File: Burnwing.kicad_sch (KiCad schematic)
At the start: 41 parts, among them J1 USB Type C, J2 Conn_01x06_MountingPin, J3 Conn_01x02_Pin, Q1 NCV8402ADDR2G, Q2 AONR21307, U1 HUSB238

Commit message: Cleaned schematic a bit
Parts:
- removed R15, R16: 750, Resistor_SMD:R_0603_1608Metric_Pad0.98x0.95mm_HandSolder, symbol Library:R
- renumbered D2 to D1, D1 to D2
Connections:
- net GND: now also D1.1 (K), D2.1 (K)
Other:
- moved on the sheet: 12V1, 1A1, 2A1, 5V1, 9V1, Burn1, Burn2, C1, C2, C3, C4, D1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

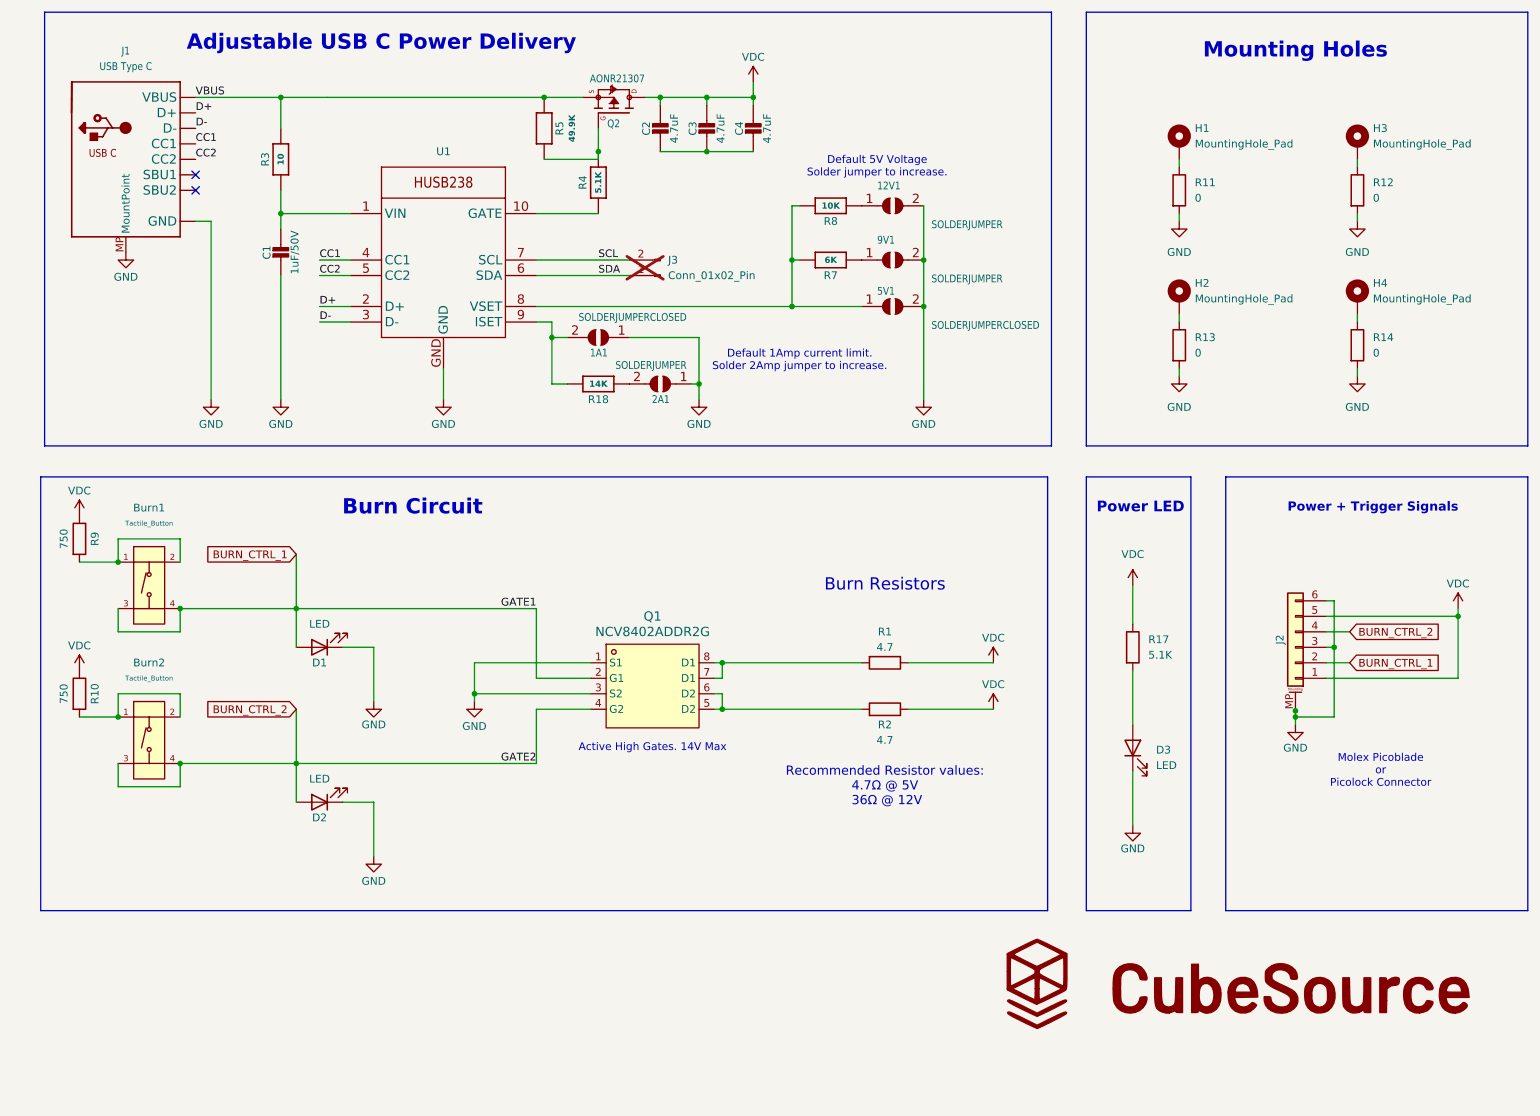
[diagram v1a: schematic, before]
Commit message: Reworked usb power and cleaned up layout
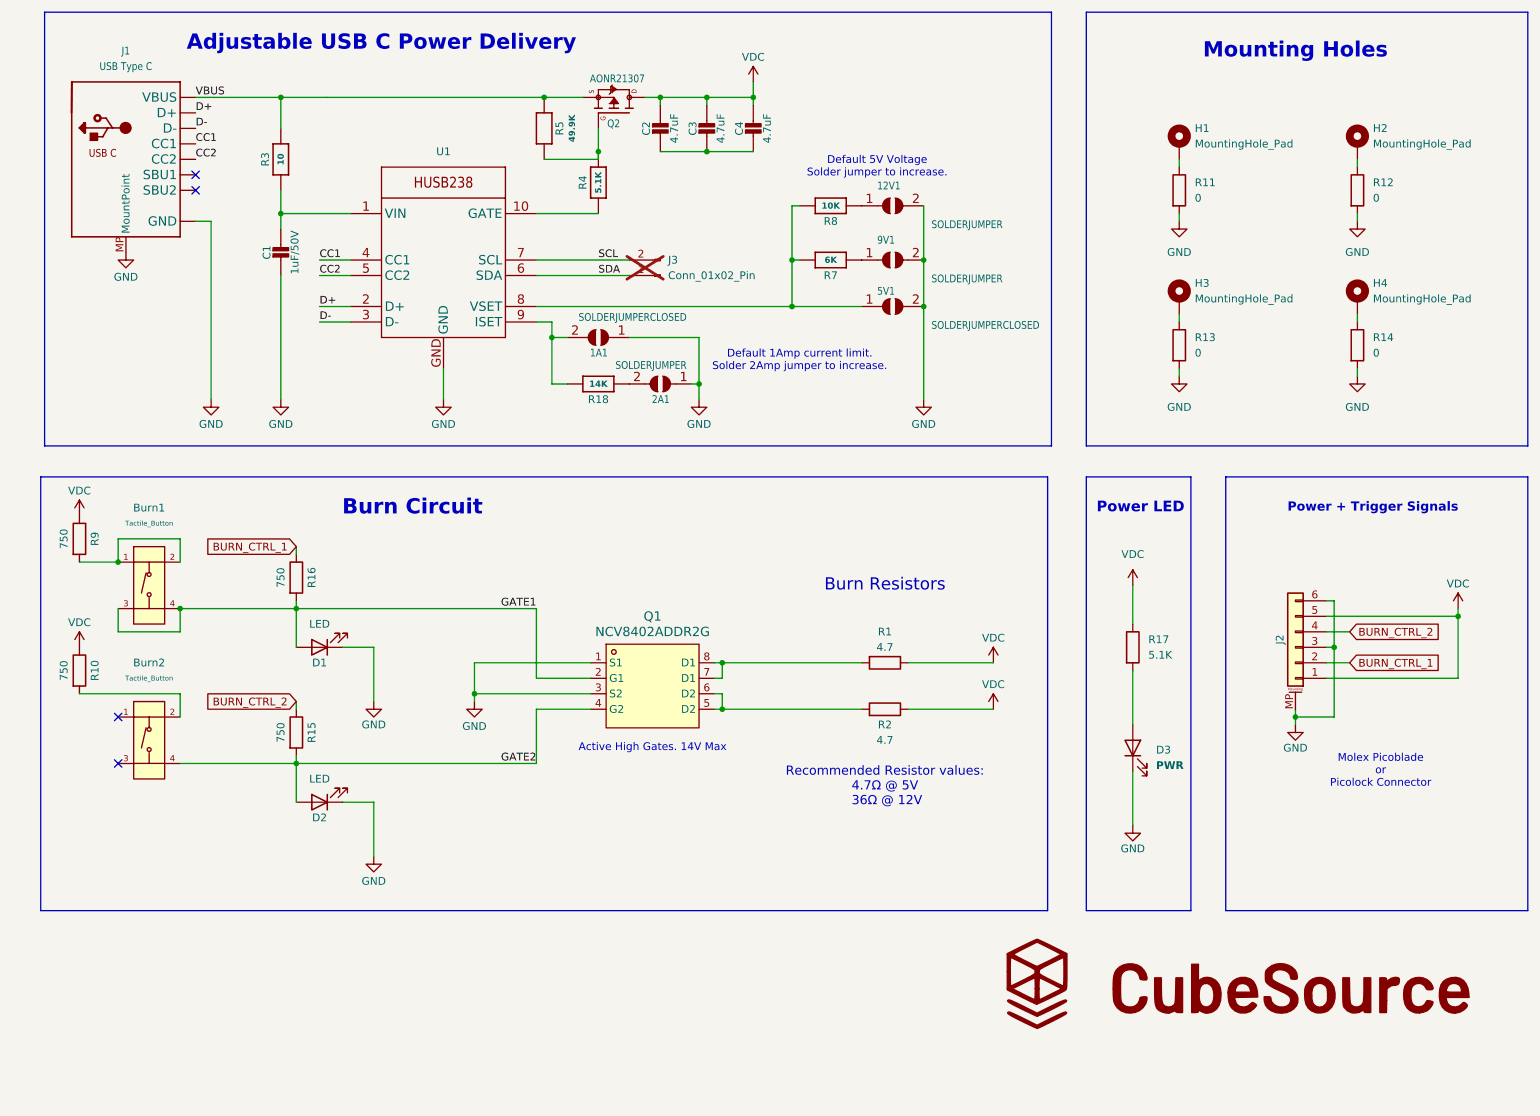
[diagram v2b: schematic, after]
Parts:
- added R15, R16: 750, Resistor_SMD:R_0603_1608Metric_Pad0.98x0.95mm_HandSolder, symbol Library:R
- D3: value LED -> PWR
- renumbered H3 to H2, H2 to H3
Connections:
- net BURN_CTRL_1: now also R16.1; no longer Burn1.3 (C), Burn1.4 (D), D1.2 (A), Q1.2 (G1)
- net BURN_CTRL_2: now also R15.1; no longer Burn2.3 (C), Burn2.4 (D), D2.2 (A), Q1.4 (G2)
- net at Burn2.2 (B), R10.2: no longer Burn2.1 (A)
- new net GATE1: Burn1.3 (C), Burn1.4 (D), D1.2 (A), Q1.2 (G1), R16.2
- new net GATE2: Burn2.4 (D), D2.2 (A), Q1.4 (G2), R15.2
- no-connect marks 2 -> 4
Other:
- moved on the sheet: R10

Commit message: Make some traces widers and added decals
Increased Trace width near R1 and R2 thru holes.

Also added decals
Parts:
- 12V1, 2A1, 9V1: footprint Adafruit HUSB238 USB-C PD Breakout:SOLDERJUMPER_ARROW_NOPASTE -> Library:SOLDERJUMPER_ARROW_NOPASTE
- 1A1, 5V1: footprint Adafruit HUSB238 USB-C PD Breakout:SOLDERJUMPER_CLOSEDWIRE -> Library:SOLDERJUMPER_CLOSEDWIRE
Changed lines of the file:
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@@
 			)
 		)
-		(property "Footprint" "Adafruit HUSB238 USB-C PD Breakout:SOLDERJUMPER_ARROW_NOPASTE"
+		(property "Footprint" "Library:SOLDERJUMPER_ARROW_NOPASTE"
 			(at 157.48 60.96 0)
 			(effects
@@
 			)
 		)
-		(property "Footprint" "Adafruit HUSB238 USB-C PD Breakout:SOLDERJUMPER_CLOSEDWIRE"
+		(property "Footprint" "Library:SOLDERJUMPER_CLOSEDWIRE"
 			(at 109.22 73.66 0)
 			(effects
@@
 			)
 		)
-		(property "Footprint" "Adafruit HUSB238 USB-C PD Breakout:SOLDERJUMPER_ARROW_NOPASTE"
+		(property "Footprint" "Library:SOLDERJUMPER_ARROW_NOPASTE"
 			(at 119.38 81.28 0)
 			(effects
@@
 			)
 		)
-		(property "Footprint" "Adafruit HUSB238 USB-C PD Breakout:SOLDERJUMPER_ARROW_NOPASTE"
+		(property "Footprint" "Library:SOLDERJUMPER_ARROW_NOPASTE"
 			(at 157.48 52.07 0)
 			(effects
@@
 			)
 		)
-		(property "Footprint" "Adafruit HUSB238 USB-C PD Breakout:SOLDERJUMPER_CLOSEDWIRE"
+		(property "Footprint" "Library:SOLDERJUMPER_CLOSEDWIRE"
 			(at 157.48 68.58 0)
 			(effects

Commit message: 4 layer v3 template
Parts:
- removed 9V1: SOLDERJUMPER, Library:SOLDERJUMPER_ARROW_NOPASTE, symbol Library:microbuilder_SOLDERJUMPER
- removed Q1: NCV8402ADDR2G, EasyEDA:SOIC-8_L4.9-W3.9-P1.27-LS6.0-BL, symbol EasyEDA:NCV8402ADDR2G
- removed R10, R9: 750, Resistor_SMD:R_0603_1608Metric_Pad0.98x0.95mm_HandSolder, symbol Library:R
- removed R7: 6K, Resistor_SMD:R_0603_1608Metric_Pad0.98x0.95mm_HandSolder, symbol Library:microbuilder_RESISTOR_0603_NOOUT
- added U2: BTS7030-2EPA, EasyEDA:PG-TSDSO-14_L4.9-W3.9-P0.65-LS6.0-BL-EP, symbol EasyEDA:BTS7030-2EPA
- Burn1, Burn2: value Tactile_Button -> KEY-SMD_4P-L6.0-W6.0-P4.50-LS9.5-BR; footprint PCM_JLCPCB:SW-SMD_4P-L5.1-W5.1-P3.70-LS6.5-TL-2 -> EasyEDA:KEY-SMD_4P-L6.0-W6.0-P4.50-LS9.5-BR; Actuator Style Round Button -> (none); Actuator/Cap Color Golden -> (none); Attrition Qty 5 -> (none); Category Switches,Tactile Switches -> (none); Circuit SPST -> (none); Class Basic Component -> (none); Contact Current 50mA -> (none); LCSC C318884 -> (none); Manufacturer XKB Connectivity -> (none); Mechanical Life 100000 Times -> (none); Minimum Qty 10 -> (none); Mounting Style Brick nogging -> (none); Operating Force 160gf -> (none); Operating Temperature -30°C~+85°C -> (none); Part TS-1187A-B-A-B -> (none); Price 0.025USD -> (none); Process SMT -> (none); Stock 433660 -> (none); Strike Gundam NO -> (none); Switch Height 1.5mm -> (none); Switch Length 5.1mm -> (none); Switch Width 5.1mm -> (none); Voltage Rating (Dc) 12V -> (none); With Lamp No -> (none)
- C1: footprint Capacitor_SMD:C_0805_2012Metric_Pad1.18x1.45mm_HandSolder -> Library:C_0805_2012Metric_Pad1.18x1.45mm_HandSolder; LCSC (none) -> C28323
- C2, C3, C4: footprint Capacitor_SMD:C_0805_2012Metric_Pad1.18x1.45mm_HandSolder -> Library:C_0805_2012Metric_Pad1.18x1.45mm_HandSolder; LCSC (none) -> C437557
- D1, D2, D3: footprint LED_SMD:LED_0603_1608Metric_Pad1.05x0.95mm_HandSolder -> Library:LED_0603_1608Metric_Pad1.05x0.95mm_HandSolder; LCSC (none) -> C94868
- H1, H2, H3, H4: footprint MountingHole:MountingHole_2.2mm_M2_Pad -> Library:MountingHole_2.2mm_M2_Pad
- J1: LCSC (none) -> C2988369
- J2: footprint Connector_Molex:Molex_PicoBlade_53261-0671_1x06-1MP_P1.25mm_Horizontal -> Library:Molex_PicoBlade_53261-0671_1x06-1MP_P1.25mm_Horizontal; Labels (none) -> +; now not fitted; now left out of the parts list
- J3: footprint Connector_PinHeader_1.00mm:PinHeader_1x02_P1.00mm_Vertical -> Library:PinHeader_1x02_P1.00mm_Vertical
- Q2: LCSC (none) -> C3277813
- R1, R2: now not fitted; now left out of the parts list
- R11: footprint Resistor_SMD:R_0603_1608Metric_Pad0.98x0.95mm_HandSolder -> Library:R_0603_1608Metric_Pad0.98x0.95mm_HandSolder; LCSC (none) -> C100044
- R12, R13, R14: footprint Resistor_SMD:R_0603_1608Metric_Pad0.98x0.95mm_HandSolder -> Library:R_0603_1608Metric_Pad0.98x0.95mm_HandSolder
- R15, R16: value 750 -> 5.1K; footprint Resistor_SMD:R_0603_1608Metric_Pad0.98x0.95mm_HandSolder -> Library:R_0603_1608Metric_Pad0.98x0.95mm_HandSolder; LCSC (none) -> C105580
- R17, R4: footprint Resistor_SMD:R_0603_1608Metric_Pad0.98x0.95mm_HandSolder -> Library:R_0603_1608Metric_Pad0.98x0.95mm_HandSolder; LCSC (none) -> C105580
- R3: footprint Resistor_SMD:R_0603_1608Metric_Pad0.98x0.95mm_HandSolder -> Library:R_0603_1608Metric_Pad0.98x0.95mm_HandSolder; LCSC (none) -> C203240
- R5: footprint Resistor_SMD:R_0603_1608Metric_Pad0.98x0.95mm_HandSolder -> Library:R_0603_1608Metric_Pad0.98x0.95mm_HandSolder; LCSC (none) -> C705780
- R7: renamed from R18; footprint Resistor_SMD:R_0603_1608Metric_Pad0.98x0.95mm_HandSolder -> Library:R_0603_1608Metric_Pad0.98x0.95mm_HandSolder; LCSC (none) -> C105580
- R8: footprint Resistor_SMD:R_0603_1608Metric_Pad0.98x0.95mm_HandSolder -> Library:R_0603_1608Metric_Pad0.98x0.95mm_HandSolder; LCSC (none) -> C95204
- U1: LCSC (none) -> C7471904
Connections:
- net BURN_CTRL_1: now also Burn1.3 (C), Burn1.4 (D), J2.3 (Pin_3), R15.1, U2.2 (IN0); no longer J2.2 (Pin_2), R16.1
- net BURN_CTRL_2: now also Burn2.3 (C), Burn2.4 (D), R16.1, U2.6 (IN1); no longer R15.1
- net GND: now also J2.1 (Pin_1), R1.1, R2.1, U2.1 (GND); no longer J2.3 (Pin_3)
- net VDC: now also Burn1.1 (A), Burn1.2 (B), Burn2.1 (A), Burn2.2 (B), J2.2 (Pin_2), U2.15 (EP); no longer J2.1 (Pin_1), R1.1, R2.1
- net at R2.2: now also U2.10 (OUT1), U2.8 (OUT1), U2.9 (OUT1)
- net at R1.2: now also U2.12 (OUT0), U2.13 (OUT0), U2.14 (OUT0)
- removed net GATE1: Burn1.3 (C), Burn1.4 (D), D1.2 (A), R16.2
- removed net GATE2: Burn2.4 (D), D2.2 (A), R15.2
- new net: D1.2 (A), R15.2
- new net: D2.2 (A), R16.2
- no-connect marks 4 -> 2
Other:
- note removed: "Active High Gates. 14V Max"
- moved on the sheet: 12V1, D1, D2, R8

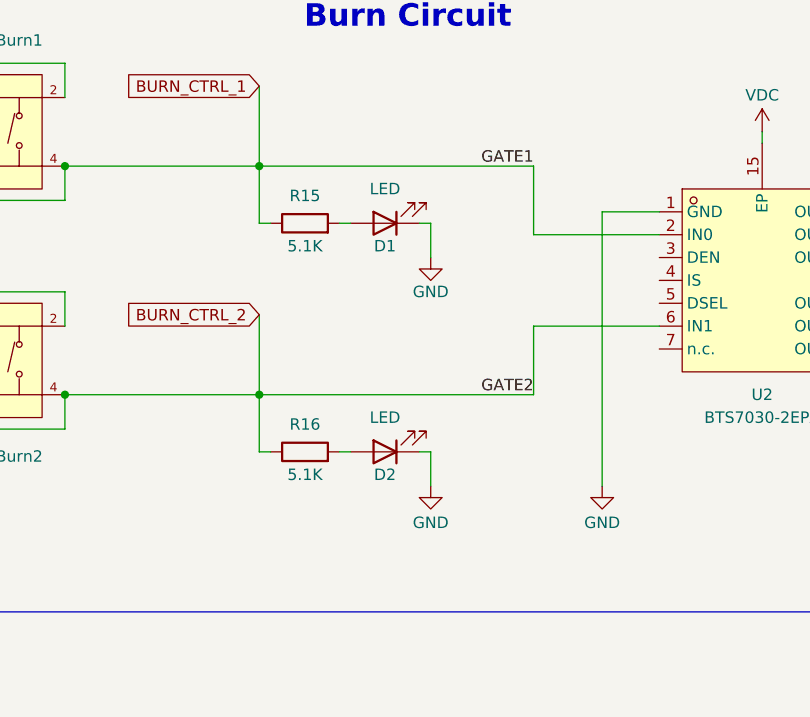
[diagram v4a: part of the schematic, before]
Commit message: added dip switch
add dip switch and adjusted layout a bit
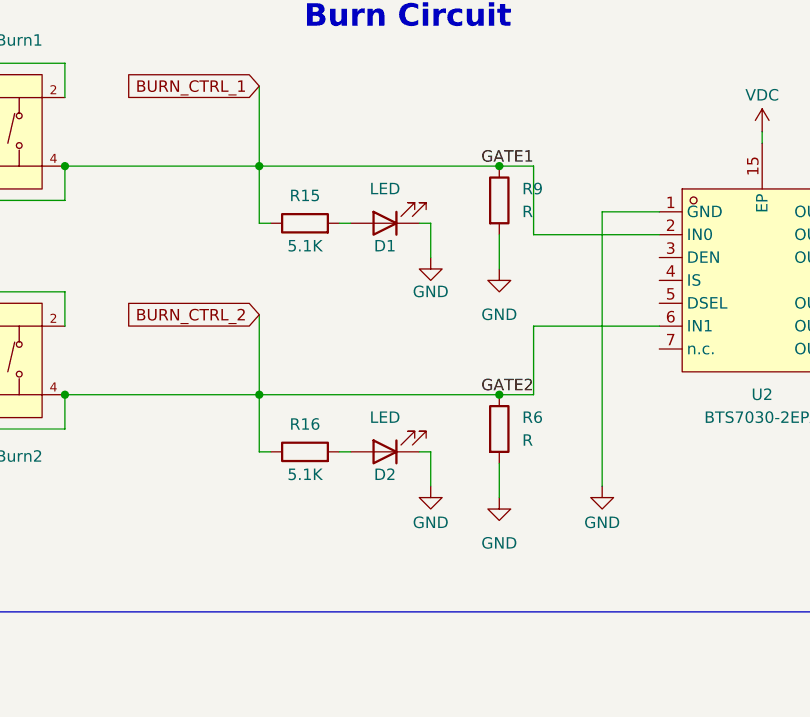
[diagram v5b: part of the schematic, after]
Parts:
- added R6, R9: R, Library:R_0603_1608Metric_Pad0.98x0.95mm_HandSolder, symbol Device:R
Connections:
- net BURN_CTRL_1: now also R9.1
- net BURN_CTRL_2: now also R6.1
- net GND: now also R6.2, R9.2
